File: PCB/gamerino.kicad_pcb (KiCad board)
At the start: 2 copper layers, 125 x 63 mm, 58 parts, among them J1 USB_B_Micro, J2 LT2, J3 RT2, P1 JOY1, P2 JOY2, P3 ICSP, P4 AUX, SW1 HATSWITCH, SW10 OPTS, SW11 X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

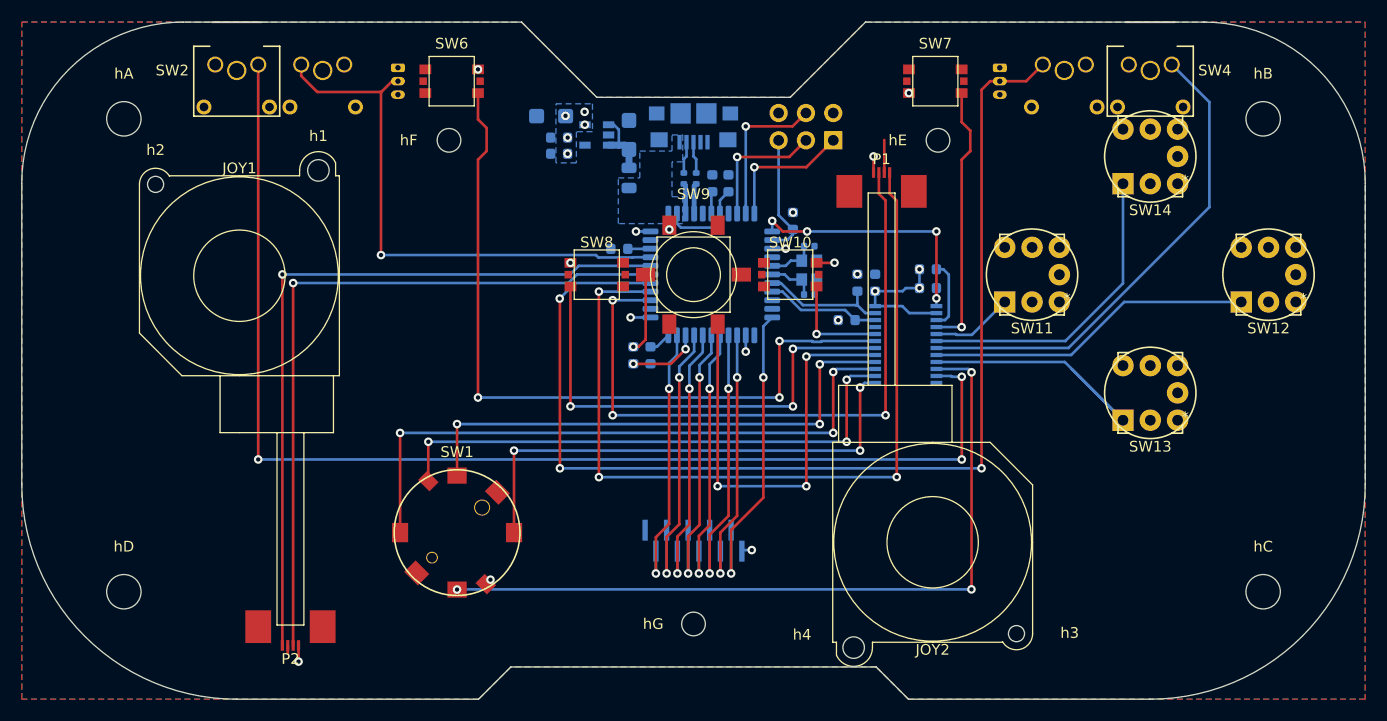
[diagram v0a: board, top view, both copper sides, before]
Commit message: Add ESD protections to analog inputs
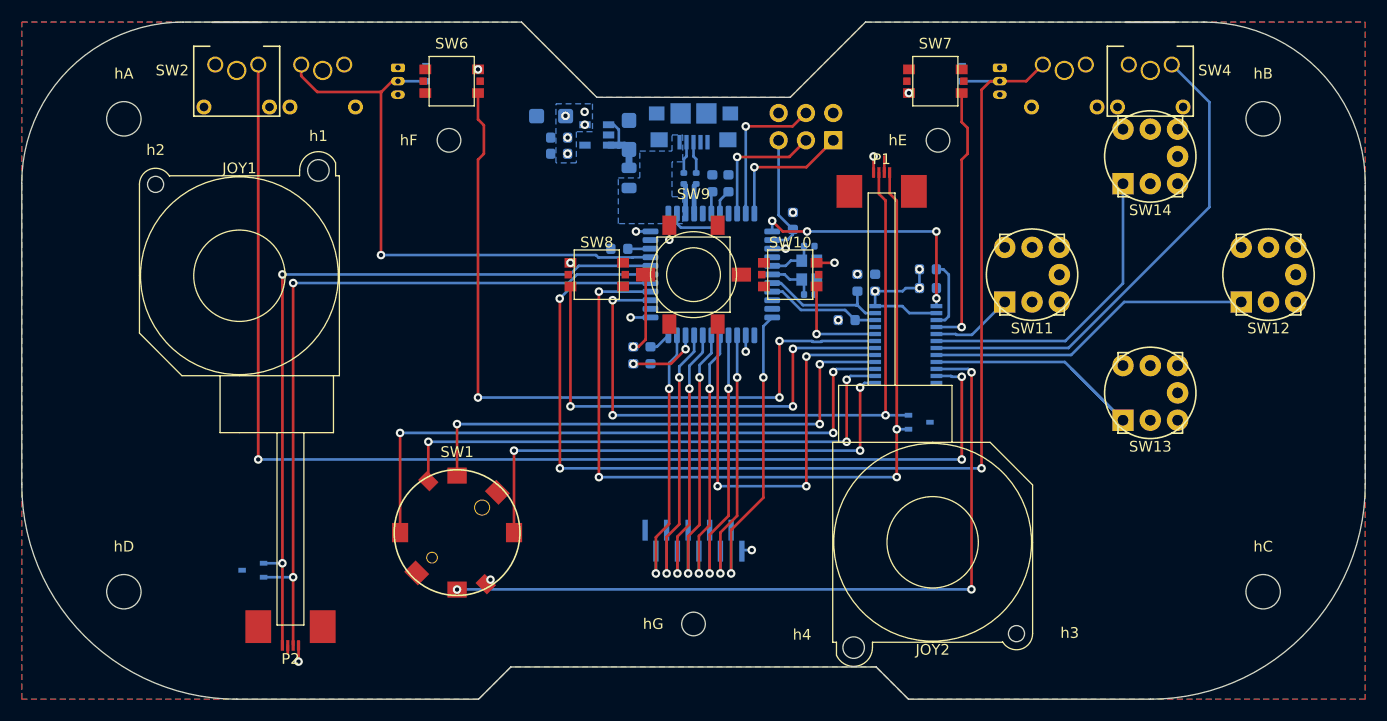
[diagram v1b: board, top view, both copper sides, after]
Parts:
- added D1: PESD5V0U1BBYL, Diode_SMD:D_SOD-523, B.Cu at (113.1, 59.3)
- added D2: PESD5V0U1BBYL, Diode_SMD:D_SOD-523, B.Cu at (163.0, 59.3)
- added D3: D5V0L2B3W, Package_TO_SOT_SMD:SOT-323_SC-70, B.Cu at (159.0, 91.7)
- added D4: D5V0L2B3W, Package_TO_SOT_SMD:SOT-323_SC-70, B.Cu at (97.0, 105.5)
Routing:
- net /RT2: track 106.0 -> 109.5 mm
- net /J2Y: track 67.3 -> 70.0 mm, vias 1 -> 2
- net /LT2: track 52.0 -> 54.6 mm
- net /J1Y: track 62.5 -> 64.6 mm
- net /J2X: track 69.1 -> 70.8 mm, vias 1 -> 2
- net +3V3: track 24.3 -> 22.8 mm
- net GND: track 5.28 -> 6.63 mm
- net /J1X: track 78.4 -> 79.5 mm, vias 3 -> 4
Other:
- rule pad_to_mask_clearance: 0.051 -> 0

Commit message: Update
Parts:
- added D5: NSR0520V2T1G, Diode_SMD:D_SOD-523, B.Cu at (181.2, 107.8)
- added D6: NSR0520V2T1G, Diode_SMD:D_SOD-523, B.Cu at (93.8, 107.5)
- added J4: ACT2, Connector_Molex:Molex_PicoBlade_53047-0210_1x02_P1.25mm_Vertical, B.Cu at (184.8, 107.8)
- added J5: ACT2, Connector_Molex:Molex_PicoBlade_53047-0210_1x02_P1.25mm_Vertical, B.Cu at (90.5, 107.5)
- added Q1: DMN601WK, Package_TO_SOT_SMD:SOT-323_SC-70, B.Cu at (181.2, 112.0)
- added Q2: DMN601WK, Package_TO_SOT_SMD:SOT-323_SC-70, B.Cu at (93.8, 112.0)
- added R10: 0R, gamerino:R_0603_1608Metric, B.Cu at (184.2, 114.5)
- added R11: 10k, gamerino:R_0603_1608Metric, B.Cu at (184.2, 113.0)
- added R12: 0R, gamerino:R_0603_1608Metric, B.Cu at (96.8, 114.5)
- added R13: 0R, gamerino:R_0603_1608Metric, B.Cu at (96.8, 113.0)
- moved D3 16.2 mm to (158.8, 75.5)
- moved R7 0.25 mm to (159.8, 77.8)
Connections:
- D3 pad 3: (no net) -> GND
- D4 pad 3: (no net) -> GND
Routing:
- net /PD3: track 0.00 -> 83.2 mm, vias 0 -> 4
- net /PD2: track 0.00 -> 75.8 mm, vias 0 -> 4
- net +3V3: track 22.8 -> 30.0 mm
- net ACT1-: track 0.00 -> 6.08 mm
- net ACT2-: track 0.00 -> 6.08 mm
- net Net-(R12-Pad1): track 0.00 -> 3.06 mm
- net Net-(R10-Pad1): track 0.00 -> 3.06 mm
- net /PD5: track 29.3 -> 30.4 mm
- net /J1Y: track 64.6 -> 64.3 mm, vias 3 -> 4

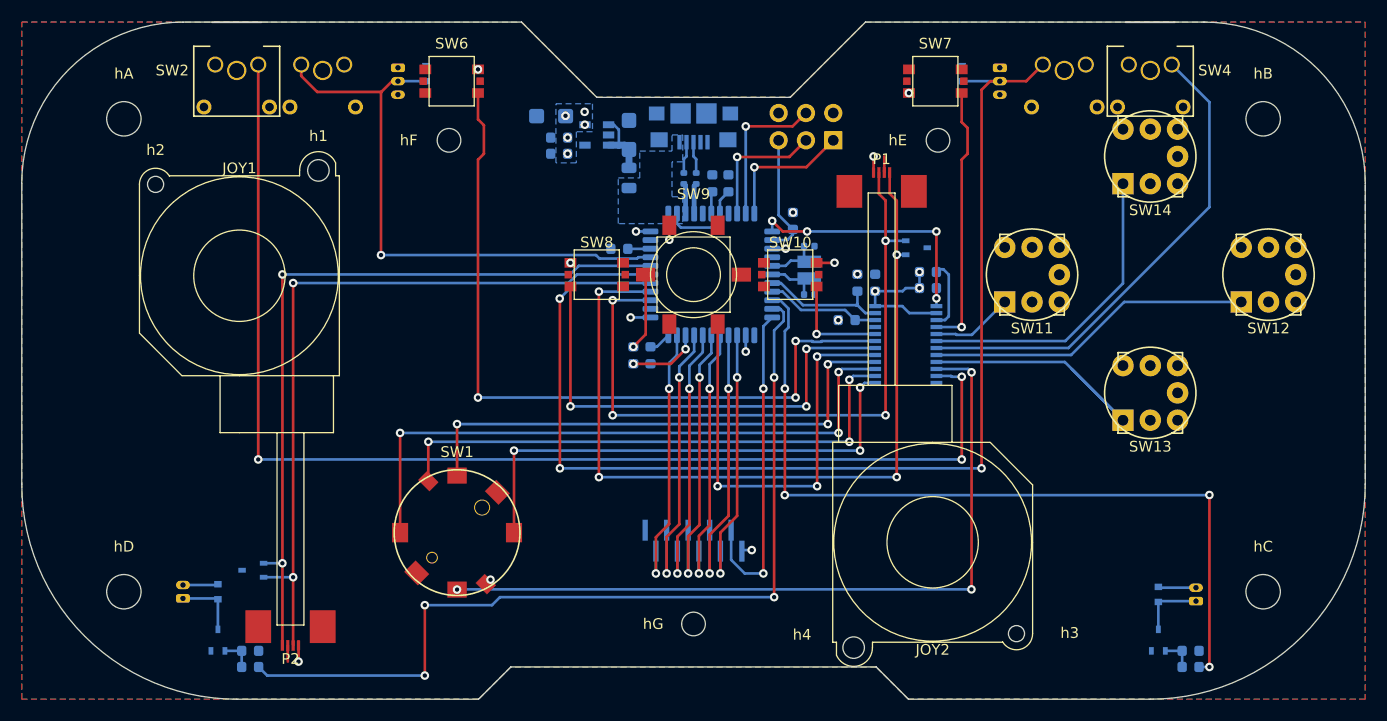
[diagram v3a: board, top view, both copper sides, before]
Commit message: Update docs, layout optimization, teardrops
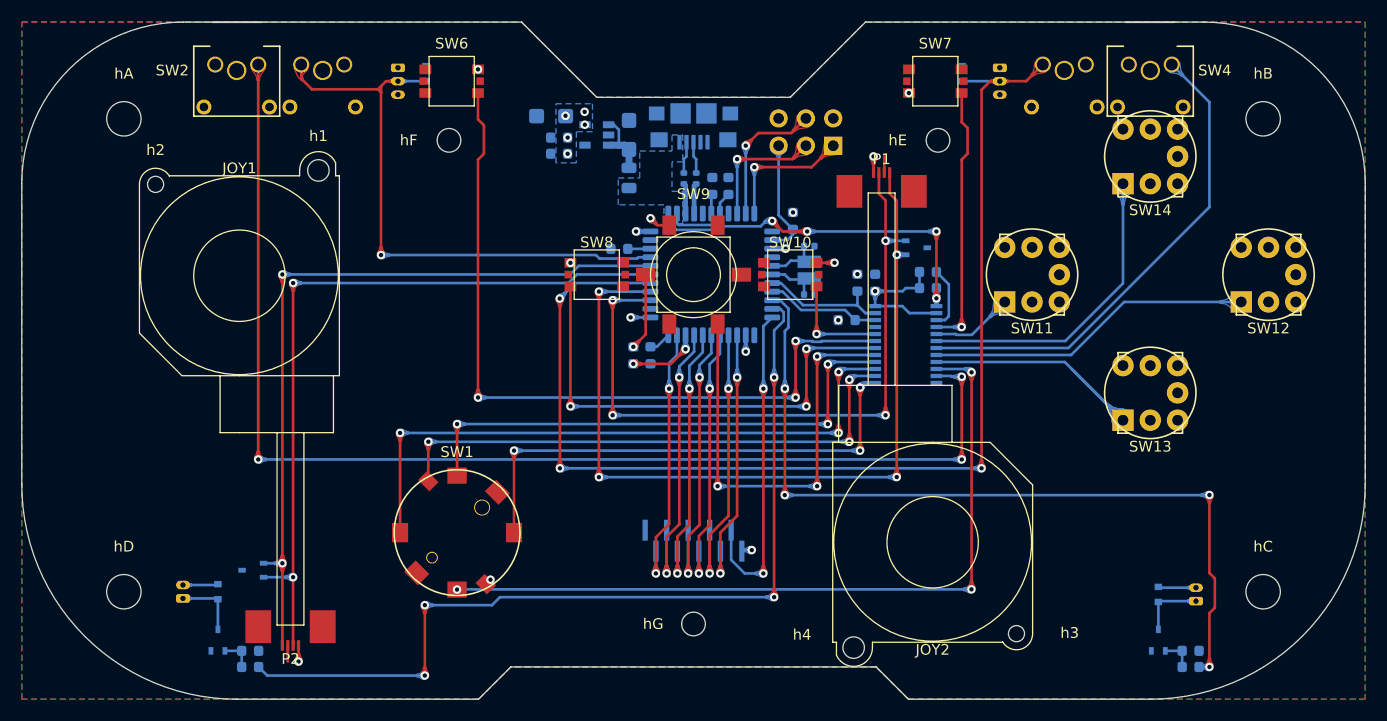
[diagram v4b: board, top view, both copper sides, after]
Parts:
- moved P3 0.50 mm to (151.0, 66.0)
- moved C8 0.25 mm to (139.8, 69.8)
- moved C9 0.25 mm to (141.2, 69.8)
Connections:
- U2 pad 1: /PE6 -> /IRQ
- U2 pad 12: /IRQ -> PB7
- U2 pad 8: (no net) -> PB0
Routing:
- net /IRQ: track 24.6 -> 34.7 mm
- net /LT2: track 54.7 -> 56.1 mm
- net /MOSI: track 14.2 -> 13.0 mm
- net GND: track 6.63 -> 7.30 mm
- net Net-(R7-Pad1): track 6.53 -> 5.90 mm
- net VBUS: track 8.53 -> 7.98 mm
- net +3V3: vias 16 -> 14

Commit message: Optimized layout
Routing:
- net /PD5: track 30.4 -> 22.0 mm
- net /PB6: track 27.1 -> 19.2 mm
- net /PD6: track 26.8 -> 18.9 mm
- net /PB4: track 26.9 -> 19.0 mm
- net /PC7: track 25.1 -> 20.9 mm
- net /PD4: track 25.0 -> 20.7 mm
- net /PB5: track 25.2 -> 21.0 mm
- net /PD7: track 25.1 -> 20.9 mm
- added copper zone on B.Cu, net /RT2
- added copper zone on F.Cu, net GND

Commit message: Update
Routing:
- net /RESET: track 11.4 -> 14.3 mm
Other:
- board text added: "01"
- board text added: "1"
- board text added: "2"
- board text added: "GAMERINO"

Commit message: Update
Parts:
- added LOGO2: OSHW-Logo, Symbol:OSHW-Logo2_7.3x6mm_SilkScreen, B.Cu at (194.0, 94.0)
- added LOGO2: LOGO-Gamerino, gamerino:gamerino_logo, B.Cu at (94.0, 94.0)
- added LOGO3: KiCad-Logo, Symbol:KiCad-Logo2_5mm_SilkScreen, F.Cu at (191.0, 95.5)
- added LOGO4: ESD-Logo, Symbol:ESD-Logo_6.6x6mm_SilkScreen, F.Cu at (85.0, 95.5)

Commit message: Update
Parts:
- P4: footprint Connector_PinSocket_1.00mm:PinSocket_1x10_P1.00mm_Vertical_SMD_Pin1Left -> gamerino:M52-5001045
- turned P4 to 0 degrees
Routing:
- net /PD4: track 20.7 -> 19.5 mm, vias 2 -> 1
- net /PB6: track 19.2 -> 20.4 mm, vias 2 -> 1
- net /PB4: track 19.0 -> 20.1 mm, vias 2 -> 1
- net /PD7: track 20.9 -> 19.9 mm, vias 2 -> 1
- net +3V3: track 30.0 -> 29.1 mm, vias 14 -> 13
- net /PD6: track 18.9 -> 19.7 mm, vias 2 -> 1
- net /PB5: track 21.0 -> 20.2 mm, vias 2 -> 1
- net /PC7: track 20.9 -> 20.3 mm, vias 2 -> 1
- net /PD5: vias 2 -> 1
